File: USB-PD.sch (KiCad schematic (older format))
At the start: 8 parts

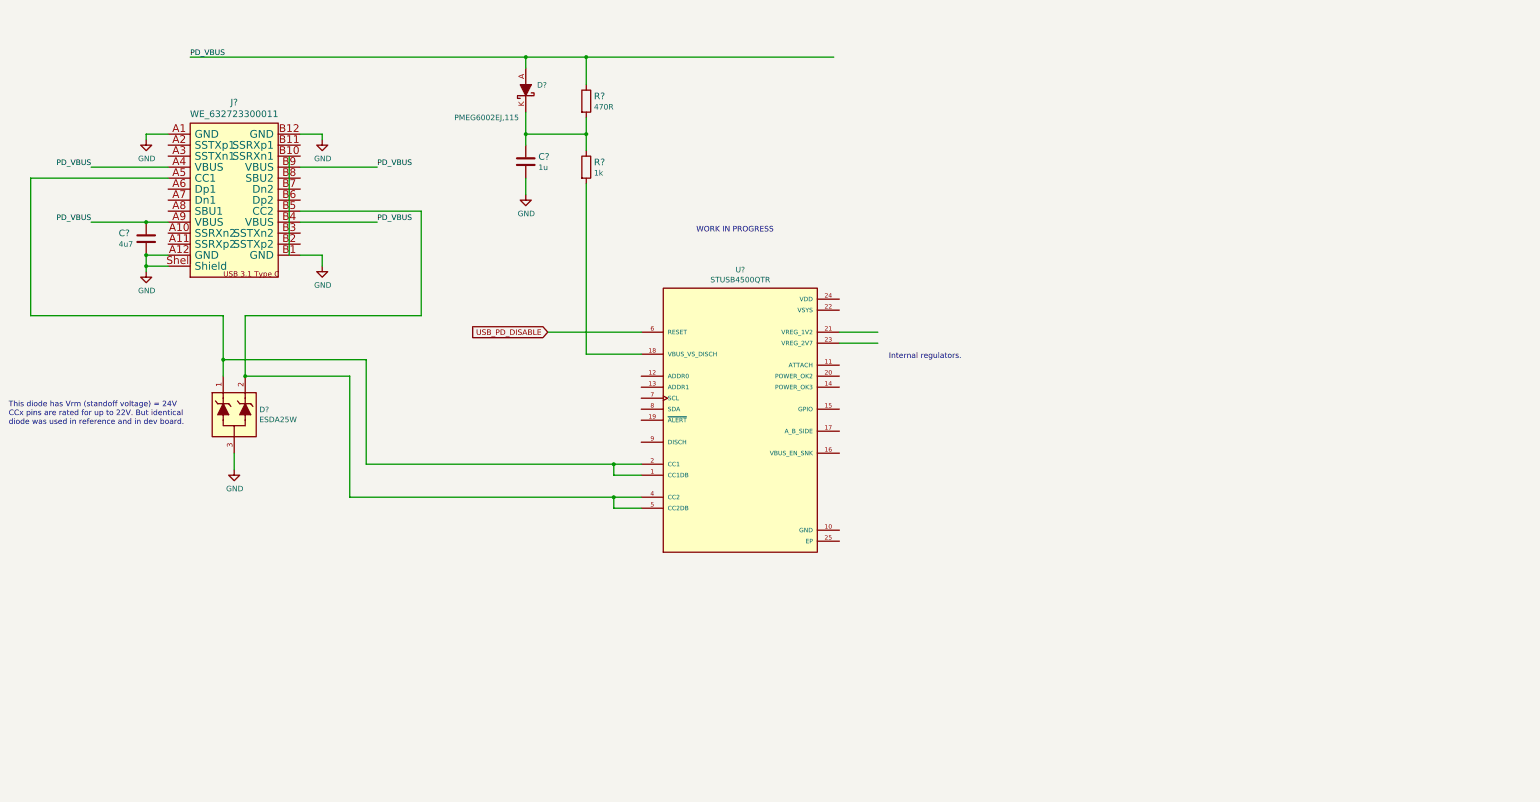
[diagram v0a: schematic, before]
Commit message: implementing USB PD - work in progress
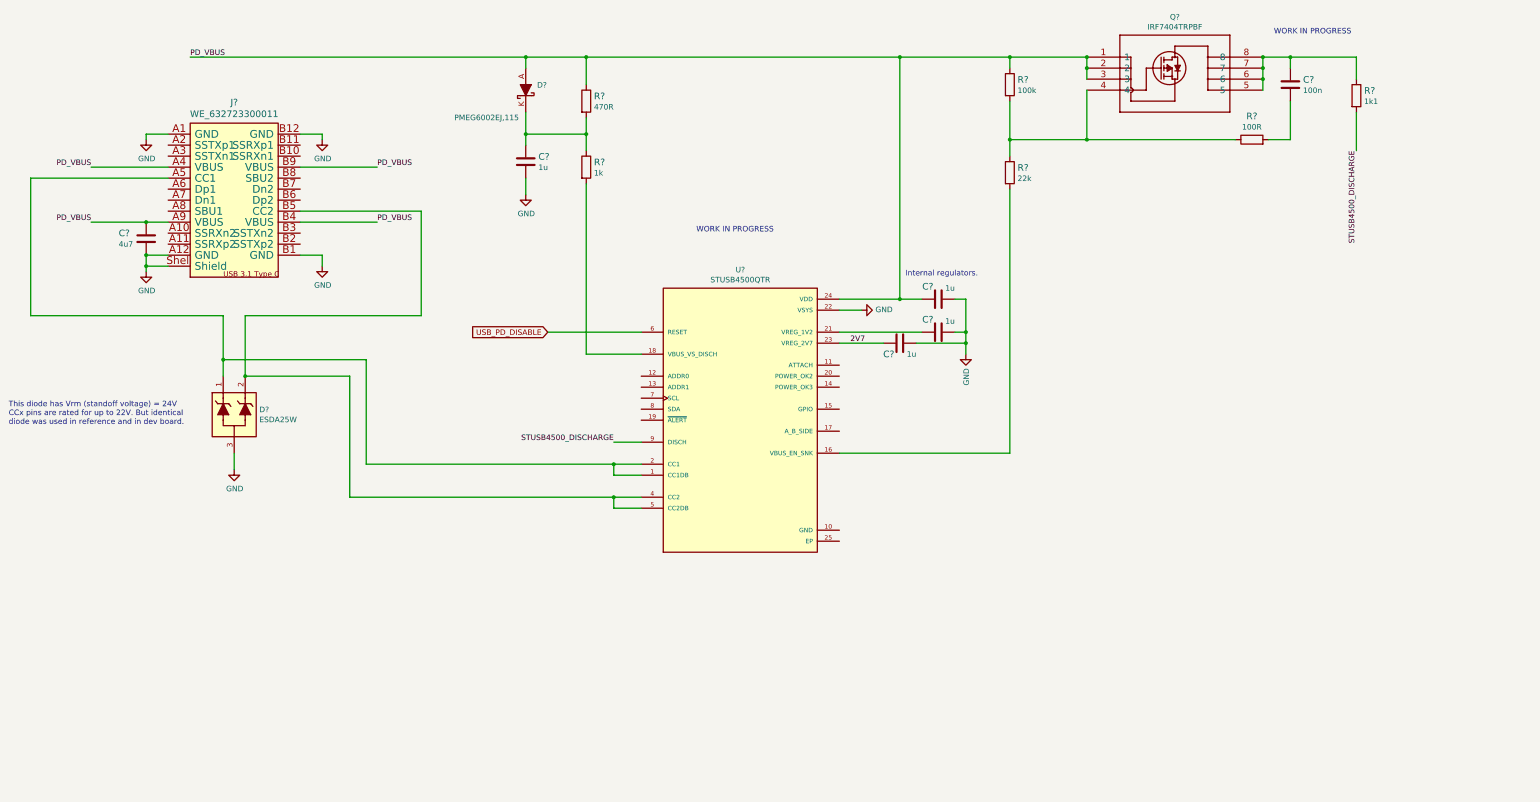
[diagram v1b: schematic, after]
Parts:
- added C? (x3): C_1u_0402, antmicro-footprints:0402-cap, symbol antmicroCapacitors0402:C_1u_0402
- added C?: C_100n_0402, antmicro-footprints:0402-cap, symbol antmicroCapacitors0402:C_100n_0402
- added Q?: IRF7404TRPBF, antmicro-footprints:IRF7416TRPBF, symbol antmicroTransistorsFETsMOSFETsSingle:IRF7404TRPBF
- added R?: R_100k_0402, antmicro-footprints:0402-res, symbol antmicroResistors0402:R_100k_0402
- added R?: R_22k_0402, antmicro-footprints:0402-res, symbol antmicroResistors0402:R_22k_0402
- added R?: R_100R_0402, antmicro-footprints:0402-res, symbol antmicroResistors0402:R_100R_0402
- added R?: R_1k1_0402, antmicro-footprints:0402-res, symbol antmicroResistors0402:R_1k1_0402
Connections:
- net labels added: 2V7, STUSB4500_DISCHARGE
- wire segments 54 -> 86

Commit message: Add USB debug circuitry, loclib
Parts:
- C127: renamed from C?; footprint antmicro-footprints:0603-cap -> sa800u-baseboard-hw-footprints:0603-cap; symbol antmicroCapacitors0603:C_4u7_0603 -> sa800u-baseboard-hw:C_4u7_0603
- C128: renamed from C?; footprint antmicro-footprints:0603-cap -> sa800u-baseboard-hw-footprints:0603-cap; symbol antmicroCapacitors0603:C_1u_0603 -> sa800u-baseboard-hw:C_1u_0603
- C? (x3): footprint antmicro-footprints:0402-cap -> sa800u-baseboard-hw-footprints:0402-cap; symbol antmicroCapacitors0402:C_1u_0402 -> sa800u-baseboard-hw:C_1u_0402
- C?: footprint antmicro-footprints:0402-cap -> sa800u-baseboard-hw-footprints:0402-cap; symbol antmicroCapacitors0402:C_100n_0402 -> sa800u-baseboard-hw:C_100n_0402
- D23: renamed from D?; footprint antmicro-footprints:SOT-323 -> sa800u-baseboard-hw-footprints:SOT-323; symbol antmicroTVSDiodes:ESDA25W -> sa800u-baseboard-hw:ESDA25W
- D24: renamed from D?; footprint antmicro-footprints:SOD-323F -> sa800u-baseboard-hw-footprints:SOD-323F; symbol antmicroDiodesRectifiersSingle:PMEG6002EJ,115 -> sa800u-baseboard-hw:PMEG6002EJ,115
- Q?: footprint antmicro-footprints:IRF7416TRPBF -> sa800u-baseboard-hw-footprints:IRF7416TRPBF; symbol antmicroTransistorsFETsMOSFETsSingle:IRF7404TRPBF -> sa800u-baseboard-hw:IRF7404TRPBF
- R106: renamed from R?; footprint antmicro-footprints:0402-res -> sa800u-baseboard-hw-footprints:0402-res; symbol antmicroResistors0402:R_470R_0402 -> sa800u-baseboard-hw:R_470R_0402
- R107: renamed from R?; footprint antmicro-footprints:0402-res -> sa800u-baseboard-hw-footprints:0402-res; symbol antmicroResistors0402:R_1k_0402 -> sa800u-baseboard-hw:R_1k_0402
- R?: footprint antmicro-footprints:0402-res -> sa800u-baseboard-hw-footprints:0402-res; symbol antmicroResistors0402:R_100k_0402 -> sa800u-baseboard-hw:R_100k_0402
- R?: footprint antmicro-footprints:0402-res -> sa800u-baseboard-hw-footprints:0402-res; symbol antmicroResistors0402:R_22k_0402 -> sa800u-baseboard-hw:R_22k_0402
- R?: footprint antmicro-footprints:0402-res -> sa800u-baseboard-hw-footprints:0402-res; symbol antmicroResistors0402:R_100R_0402 -> sa800u-baseboard-hw:R_100R_0402
- R?: footprint antmicro-footprints:0402-res -> sa800u-baseboard-hw-footprints:0402-res; symbol antmicroResistors0402:R_1k1_0402 -> sa800u-baseboard-hw:R_1k1_0402
- U18: renamed from U?; footprint antmicro-footprints:QFN50P400X400X90-25N -> sa800u-baseboard-hw-footprints:QFN50P400X400X90-25N; symbol antmicroPMICPowerDistributionSwitchesLoadDrivers:STUSB4500QTR -> sa800u-baseboard-hw:STUSB4500QTR
- gave numbers to parts that had none: 1

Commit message: Anotate parts
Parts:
- gave numbers to parts that had none: 8
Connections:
- wire segments 86 -> 83
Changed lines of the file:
@@
 WORK IN PROGRESS
 $Comp
-L sa800u-baseboard-hw:GND #PWR?
+L sa800u-baseboard-hw:GND #PWR0213
 U 1 1 61DF321E
 P 9650 4450
-F 0 "#PWR?" H 9650 4200 50  0001 C CNN
+F 0 "#PWR0213" H 9650 4200 50  0001 C CNN
 F 1 "GND" V 9655 4322 50  0000 R CNN
 F 2 "" H 9650 4450 50  0001 C CNN
@@
 $EndComp
 $Comp
-L sa800u-baseboard-hw:C_1u_0402 C?
+L sa800u-baseboard-hw:C_1u_0402 C136
 U 1 1 61DF393A
 P 9050 4350
-F 0 "C?" V 8950 4400 60  0000 L CNN
+F 0 "C136" V 8950 4400 60  0000 L CNN
 F 1 "C_1u_0402" H 9050 4200 60  0001 C CNN
 F 2 "sa800u-baseboard-hw-footprints:0402-cap" H 9250 4550 60  0001 L CNN
@@
 $EndComp
 $Comp
-L sa800u-baseboard-hw:C_1u_0402 C?
+L sa800u-baseboard-hw:C_1u_0402 C138
 U 1 1 61DF5A13
 P 9400 4250
-F 0 "C?" V 9515 4295 60  0000 L CNN
+F 0 "C138" V 9515 4295 60  0000 L CNN
 F 1 "C_1u_0402" H 9400 4100 60  0001 C CNN
 F 2 "sa800u-baseboard-hw-footprints:0402-cap" H 9600 4450 60  0001 L CNN
@@
 Connection ~ 9650 4250
 $Comp
-L sa800u-baseboard-hw:GND #PWR?
+L sa800u-baseboard-hw:GND #PWR0214
 U 1 1 61E0C3B2
 P 8700 4050
-F 0 "#PWR?" H 8700 3800 50  0001 C CNN
+F 0 "#PWR0214" H 8700 3800 50  0001 C CNN
 F 1 "GND" V 8705 3922 50  0000 R CNN
 F 2 "" H 8700 4050 50  0001 C CNN
@@
 	6200 1750 9050 1750
 $Comp
-L sa800u-baseboard-hw:C_1u_0402 C?
+L sa800u-baseboard-hw:C_1u_0402 C137
 U 1 1 61E26115
 P 9400 3950
-F 0 "C?" V 9515 3995 60  0000 L CNN
+F 0 "C137" V 9515 3995 60  0000 L CNN
 F 1 "C_1u_0402" H 9400 3800 60  0001 C CNN
 F 2 "sa800u-baseboard-hw-footprints:0402-cap" H 9600 4150 60  0001 L CNN
@@
 $EndComp
 Wire Wire Line
-	10750 1750 10750 1850
-Connection ~ 10750 1850
-Wire Wire Line
-	10750 1850 10750 1950
-Wire Wire Line
 	10750 1750 10050 1750
-Connection ~ 10750 1750
-Wire Wire Line
-	12350 1750 12350 1850
-Connection ~ 12350 1850
-Wire Wire Line
-	12350 1850 12350 1950
-Connection ~ 12350 1950
-Wire Wire Line
-	12350 1950 12350 2050
-$Comp
-L sa800u-baseboard-hw:R_100k_0402 R?
+$Comp
+L sa800u-baseboard-hw:R_100k_0402 R108
 U 1 1 61E6364D
 P 10050 2000
-F 0 "R?" V 10005 2070 60  0000 L CNN
+F 0 "R108" V 10005 2070 60  0000 L CNN
 F 1 "R_100k_0402" H 10050 1850 60  0001 C CNN
 F 2 "sa800u-baseboard-hw-footprints:0402-res" H 10250 2200 60  0001 L CNN
@@
 Connection ~ 10050 1750
 $Comp
-L sa800u-baseboard-hw:R_22k_0402 R?
+L sa800u-baseboard-hw:R_22k_0402 R109
 U 1 1 61E675D2
 P 10050 2800
-F 0 "R?" V 10005 2870 60  0000 L CNN
+F 0 "R109" V 10005 2870 60  0000 L CNN
 F 1 "R_22k_0402" H 10050 2650 60  0001 C CNN
 F 2 "sa800u-baseboard-hw-footprints:0402-res" H 10250 3000 60  0001 L CNN
@@
 Wire Wire Line
 	12350 1750 12600 1750
-Connection ~ 12350 1750
 Wire Wire Line
 	12600 1750 12600 1850
@@
 Connection ~ 10750 2500
 $Comp
-L sa800u-baseboard-hw:C_100n_0402 C?
+L sa800u-baseboard-hw:C_100n_0402 C139
 U 1 1 61E6EBE7
 P 12600 2000
-F 0 "C?" H 12715 2045 60  0000 L CNN
+F 0 "C139" H 12715 2045 60  0000 L CNN
 F 1 "C_100n_0402" H 12600 1850 60  0001 C CNN
 F 2 "sa800u-baseboard-hw-footprints:0402-cap" H 12800 2200 60  0001 L CNN
@@
 $EndComp
 $Comp
-L sa800u-baseboard-hw:R_100R_0402 R?
+L sa800u-baseboard-hw:R_100R_0402 R110
 U 1 1 61E6F64B
 P 12250 2500
-F 0 "R?" H 12250 2713 60  0000 C CNN
+F 0 "R110" H 12250 2713 60  0000 C CNN
 F 1 "R_100R_0402" H 12250 2350 60  0001 C CNN
 F 2 "sa800u-baseboard-hw-footprints:0402-res" H 12450 2700 60  0001 L CNN
@@
 	12600 1750 13200 1750
 $Comp
-L sa800u-baseboard-hw:R_1k1_0402 R?
+L sa800u-baseboard-hw:R_1k1_0402 R111
 U 1 1 61E821E4
 P 13200 2100
-F 0 "R?" V 13155 2170 60  0000 L CNN
+F 0 "R111" V 13155 2170 60  0000 L CNN
 F 1 "R_1k1_0402" H 13200 1950 60  0001 C CNN
 F 2 "sa800u-baseboard-hw-footprints:0402-res" H 13400 2300 60  0001 L CNN
@@
 Text Notes 12450 1550 0    50   ~ 0
 WORK IN PROGRESS
+Wire Wire Line
+	10750 1750 10750 1950
+Wire Wire Line
+	12350 1750 12350 2050
 $EndSCHEMATC

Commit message: Anotate parts
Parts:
- Q7: renamed from Q?; symbol sa800u-baseboard-hw:IRF7404TRPBF -> sa800u-baseboard-hw:IRF7416TRPBF
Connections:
- wire segments 83 -> 86
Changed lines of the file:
@@
 Connection ~ 9650 4350
 $Comp
-L sa800u-baseboard-hw:IRF7404TRPBF Q?
+L sa800u-baseboard-hw:IRF7416TRPBF Q7
 U 1 1 61E557F1
 P 11550 1900
-F 0 "Q?" H 11550 2415 50  0000 C CNN
+F 0 "Q7" H 11550 2415 50  0000 C CNN
 F 1 "IRF7404TRPBF" H 11550 2324 50  0000 C CNN
 F 2 "sa800u-baseboard-hw-footprints:IRF7416TRPBF" H 11530 2295 50  0001 C CNN
@@
 WORK IN PROGRESS
 Wire Wire Line
-	10750 1750 10750 1950
+	12350 1750 12350 1850
 Wire Wire Line
-	12350 1750 12350 2050
+	10750 1850 10750 1950
+Wire Wire Line
+	12350 1950 12350 2050
+Connection ~ 12350 1750
+Wire Wire Line
+	10750 1850 10750 1750
+Connection ~ 10750 1850
+Connection ~ 10750 1750
+Wire Wire Line
+	12350 1950 12350 1850
+Connection ~ 12350 1950
+Connection ~ 12350 1850
 $EndSCHEMATC

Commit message: add output TVS diode supplement ESD144B1W0201E6327XTSA1
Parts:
- added D?: ESD144B1W0201E6327XTSA1, antmicro-footprints:ESD144B1W0201E6327XTSA1, symbol antmicroTVSDiodes:ESD144B1W0201E6327XTSA1
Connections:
- net labels added: VDD
- wire segments 86 -> 90
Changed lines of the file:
@@
 $Descr A3 16535 11693
 encoding utf-8
-Sheet 12 13
+Sheet 12 12
 Title ""
 Date ""
@@
 Connection ~ 12350 1950
 Connection ~ 12350 1850
+$Comp
+L antmicroTVSDiodes:ESD144B1W0201E6327XTSA1 D?
+U 1 1 61ED3FD6
+P 14050 2150
+F 0 "D?" V 14004 2228 50  0000 L CNN
+F 1 "ESD144B1W0201E6327XTSA1" V 14095 2228 50  0000 L CNN
+F 2 "antmicro-footprints:ESD144B1W0201E6327XTSA1" H 14050 2150 50  0001 C CNN
+F 3 "https://www.infineon.com/dgdl/Infineon-ESD144-B1-W0201-DataSheet-v02_00-EN.pdf?fileId=5546d462677d0f4601679886a2a8707c" H 14050 2150 50  0001 C CNN
+F 4 "ESD144B1W0201E6327XTSA1" H 14050 2150 50  0001 C CNN "MPN"
+F 5 "Infineon Technologies" H 14050 2150 50  0001 C CNN "Manufacturer"
+	1    14050 2150
+	0    1    1    0
+$EndComp
+Wire Wire Line
+	13200 1750 14050 1750
+Wire Wire Line
+	14050 1750 14050 1800
+Connection ~ 13200 1750
+Wire Wire Line
+	14050 2500 14050 2550
+$Comp
+L power:GND #PWR?
+U 1 1 61EDB438
+P 14050 2550
+F 0 "#PWR?" H 14050 2300 50  0001 C CNN
+F 1 "GND" H 14055 2377 50  0000 C CNN
+F 2 "" H 14050 2550 50  0001 C CNN
+F 3 "" H 14050 2550 50  0001 C CNN
+	1    14050 2550
+	1    0    0    -1
+$EndComp
+Wire Wire Line
+	14050 1750 14500 1750
+Connection ~ 14050 1750
+Text GLabel 14500 1750 2    50   Input ~ 0
+VDD
 $EndSCHEMATC

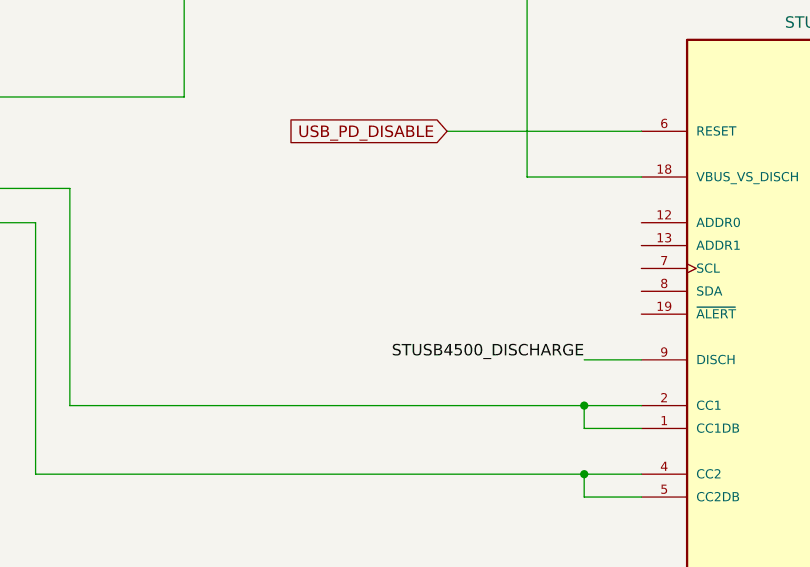
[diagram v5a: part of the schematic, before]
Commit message: add I2C address selection circuit
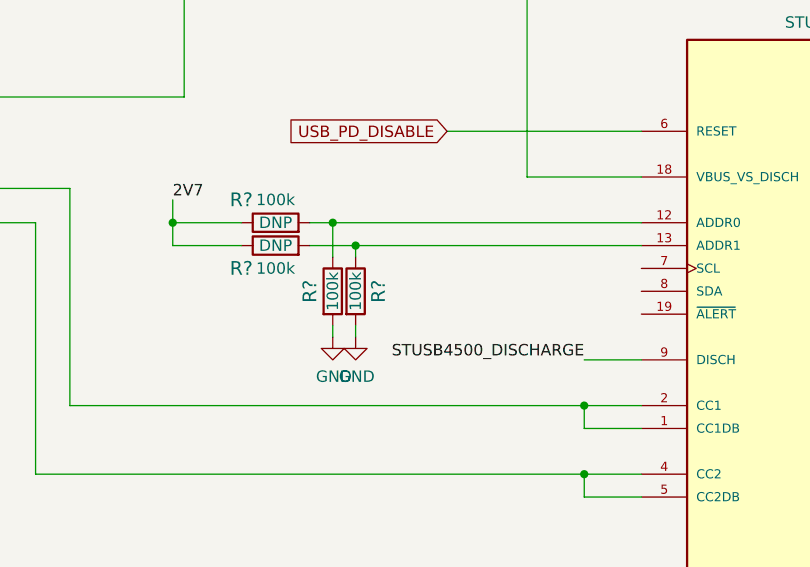
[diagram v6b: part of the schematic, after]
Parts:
- added R? (x4): R_100k_0402, antmicro-footprints:0402-res, symbol antmicroResistors0402:R_100k_0402
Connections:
- wire segments 90 -> 102
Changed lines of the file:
@@
 Text GLabel 14500 1750 2    50   Input ~ 0
 VDD
+Wire Wire Line
+	4650 4650 4650 4550
+Wire Wire Line
+	4650 4650 4650 4750
+Wire Wire Line
+	4650 4750 4950 4750
+Connection ~ 4650 4650
+Text Label 4650 4550 0    50   ~ 0
+2V7
+$Comp
+L antmicroResistors0402:R_100k_0402 R?
+U 1 1 61EEDDB8
+P 5100 4650
+F 0 "R?" H 4950 4750 60  0000 C CNN
+F 1 "R_100k_0402" H 5100 4500 60  0001 C CNN
+F 2 "antmicro-footprints:0402-res" H 5300 4850 60  0001 L CNN
+F 3 "" H 5100 4650 50  0001 C CNN
+F 4 "VISHAY" H 5300 5050 60  0001 L CNN "Manufacturer"
+F 5 "CRCW0402100KFKEDHP" H 5300 4950 60  0001 L CNN "MPN"
+F 6 "100k" H 5100 4750 50  0000 C CNN "Val"
+F 7 "DNP" H 5100 4650 50  0000 C CNN "DNP"
+	1    5100 4650
+	1    0    0    -1
+$EndComp
+Wire Wire Line
+	4950 4650 4650 4650
+$Comp
+L antmicroResistors0402:R_100k_0402 R?
+U 1 1 61EEE353
+P 5100 4750
+F 0 "R?" H 4950 4650 60  0000 C CNN
+F 1 "R_100k_0402" H 5100 4600 60  0001 C CNN
+F 2 "antmicro-footprints:0402-res" H 5300 4950 60  0001 L CNN
+F 3 "" H 5100 4750 50  0001 C CNN
+F 4 "VISHAY" H 5300 5150 60  0001 L CNN "Manufacturer"
+F 5 "CRCW0402100KFKEDHP" H 5300 5050 60  0001 L CNN "MPN"
+F 6 "100k" H 5100 4650 50  0000 C CNN "Val"
+F 7 "DNP" H 5100 4750 50  0000 C CNN "DNP"
+	1    5100 4750
+	1    0    0    -1
+$EndComp
+Wire Wire Line
+	5250 4750 5450 4750
+Wire Wire Line
+	5350 4650 5350 4800
+Connection ~ 5350 4650
+Wire Wire Line
+	5350 4650 5250 4650
+Wire Wire Line
+	5450 4750 5450 4800
+Connection ~ 5450 4750
+$Comp
+L power:GND #PWR?
+U 1 1 61EF35F3
+P 5350 5150
+F 0 "#PWR?" H 5350 4900 50  0001 C CNN
+F 1 "GND" H 5355 4977 50  0000 C CNN
+F 2 "" H 5350 5150 50  0001 C CNN
+F 3 "" H 5350 5150 50  0001 C CNN
+	1    5350 5150
+	1    0    0    -1
+$EndComp
+$Comp
+L power:GND #PWR?
+U 1 1 61EF3823
+P 5450 5150
+F 0 "#PWR?" H 5450 4900 50  0001 C CNN
+F 1 "GND" H 5455 4977 50  0000 C CNN
+F 2 "" H 5450 5150 50  0001 C CNN
+F 3 "" H 5450 5150 50  0001 C CNN
+	1    5450 5150
+	1    0    0    -1
+$EndComp
+$Comp
+L antmicroResistors0402:R_100k_0402 R?
+U 1 1 61EF8DE3
+P 5350 4950
+F 0 "R?" H 5350 4850 60  0000 C CNN
+F 1 "R_100k_0402" H 5350 4800 60  0001 C CNN
+F 2 "antmicro-footprints:0402-res" H 5550 5150 60  0001 L CNN
+F 3 "" H 5350 4950 50  0001 C CNN
+F 4 "VISHAY" H 5550 5350 60  0001 L CNN "Manufacturer"
+F 5 "CRCW0402100KFKEDHP" H 5550 5250 60  0001 L CNN "MPN"
+F 6 "100k" H 5350 4950 50  0000 C CNN "Val"
+	1    5350 4950
+	0    1    1    0
+$EndComp
+Wire Wire Line
+	5350 5100 5350 5150
+$Comp
+L antmicroResistors0402:R_100k_0402 R?
+U 1 1 61F02819
+P 5450 4950
+F 0 "R?" H 5450 5050 60  0000 C CNN
+F 1 "R_100k_0402" H 5450 4800 60  0001 C CNN
+F 2 "antmicro-footprints:0402-res" H 5650 5150 60  0001 L CNN
+F 3 "" H 5450 4950 50  0001 C CNN
+F 4 "VISHAY" H 5650 5350 60  0001 L CNN "Manufacturer"
+F 5 "CRCW0402100KFKEDHP" H 5650 5250 60  0001 L CNN "MPN"
+F 6 "100k" H 5450 4950 50  0000 C CNN "Val"
+	1    5450 4950
+	0    1    1    0
+$EndComp
+Wire Wire Line
+	5450 5100 5450 5150
+Wire Wire Line
+	5350 4650 6700 4650
+Wire Wire Line
+	5450 4750 6700 4750
 $EndSCHEMATC

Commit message: add i2c pullups
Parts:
- added R? (x2): R_4k7_0402, antmicro-footprints:0402-res, symbol antmicroResistors0402:R_4k7_0402
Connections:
- net labels added: 1V8, STUSB4500_SCL, STUSB4500_SDA
- wire segments 102 -> 114
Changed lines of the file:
@@
 Wire Wire Line
 	5450 4750 6700 4750
+Wire Wire Line
+	8500 6050 8850 6050
+Wire Wire Line
+	8850 6050 8850 6150
+Wire Wire Line
+	8500 6150 8850 6150
+Connection ~ 8850 6150
+$Comp
+L power:GND #PWR?
+U 1 1 61F1871C
+P 8850 6250
+F 0 "#PWR?" H 8850 6000 50  0001 C CNN
+F 1 "GND" H 8855 6077 50  0000 C CNN
+F 2 "" H 8850 6250 50  0001 C CNN
+F 3 "" H 8850 6250 50  0001 C CNN
+	1    8850 6250
+	1    0    0    -1
+$EndComp
+Wire Wire Line
+	8850 6150 8850 6250
+Text GLabel 6350 4950 0    50   Input ~ 0
+STUSB4500_SDA
+Text GLabel 6350 4850 0    50   Input ~ 0
+STUSB4500_SCL
+Wire Wire Line
+	6350 4850 6700 4850
+Wire Wire Line
+	6350 4950 6700 4950
+Text GLabel 5000 6400 0    50   Input ~ 0
+STUSB4500_SDA
+Text GLabel 5000 6300 0    50   Input ~ 0
+STUSB4500_SCL
+Wire Wire Line
+	5000 6300 5200 6300
+Wire Wire Line
+	5750 6300 5750 6150
+Wire Wire Line
+	5850 6400 5850 6150
+Wire Wire Line
+	5000 6400 5200 6400
+Text GLabel 5750 6150 1    50   Input ~ 0
+1V8
+Text GLabel 5850 6150 1    50   Input ~ 0
+1V8
+$Comp
+L antmicroResistors0402:R_4k7_0402 R?
+U 1 1 61F8049E
+P 5350 6300
+F 0 "R?" H 5350 6513 60  0000 C CNN
+F 1 "R_4k7_0402" H 5350 6150 60  0001 C CNN
+F 2 "antmicro-footprints:0402-res" H 5550 6500 60  0001 L CNN
+F 3 "" H 5350 6300 50  0001 C CNN
+F 4 "VISHAY" H 5550 6700 60  0001 L CNN "Manufacturer"
+F 5 "MCS04020C4701FE000" H 5550 6600 60  0001 L CNN "MPN"
+F 6 "4k7" H 5350 6415 50  0000 C CNN "Val"
+	1    5350 6300
+	1    0    0    -1
+$EndComp
+Wire Wire Line
+	5500 6300 5750 6300
+$Comp
+L antmicroResistors0402:R_4k7_0402 R?
+U 1 1 61F80835
+P 5350 6400
+F 0 "R?" H 5350 6200 60  0000 C CNN
+F 1 "R_4k7_0402" H 5350 6250 60  0001 C CNN
+F 2 "antmicro-footprints:0402-res" H 5550 6600 60  0001 L CNN
+F 3 "" H 5350 6400 50  0001 C CNN
+F 4 "VISHAY" H 5550 6800 60  0001 L CNN "Manufacturer"
+F 5 "MCS04020C4701FE000" H 5550 6700 60  0001 L CNN "MPN"
+F 6 "4k7" H 5350 6300 50  0000 C CNN "Val"
+	1    5350 6400
+	1    0    0    -1
+$EndComp
+Wire Wire Line
+	5500 6400 5850 6400
 $EndSCHEMATC
